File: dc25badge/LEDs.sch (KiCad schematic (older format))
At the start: 72 parts, among them U10 APA102, U11 APA102, U12 APA102, U13 APA102, U14 APA102, U15 APA102, U16 APA102, U17 APA102, U18 APA102, U19 APA102, U20 APA102, U21 APA102, U22 APA102, U23 APA102, U24 APA102, U25 APA102, U26 APA102, U27 APA102, U28 APA102, U29 APA102, U30 APA102, U31 APA102, U32 APA102, U33 APA102, U34 APA102, U35 APA102, U36 APA102, U37 APA102, U38 APA102, U39 APA102, U40 APA102, U41 APA102, U42 APA102, U43 APA102, U44 APA102, U45 APA102, U46 APA102, U47 APA102, U48 APA102, U49 APA102, U5 APA102, U50 APA102, U51 APA102, U52 APA102, U53 APA102, U54 APA102, U55 APA102, U56 APA102, U57 APA102, U58 APA102, U59 APA102, U6 APA102, U60 APA102, U61 APA102, U62 APA102, U63 APA102, U64 APA102, U7 APA102, U8 APA102, U9 APA102

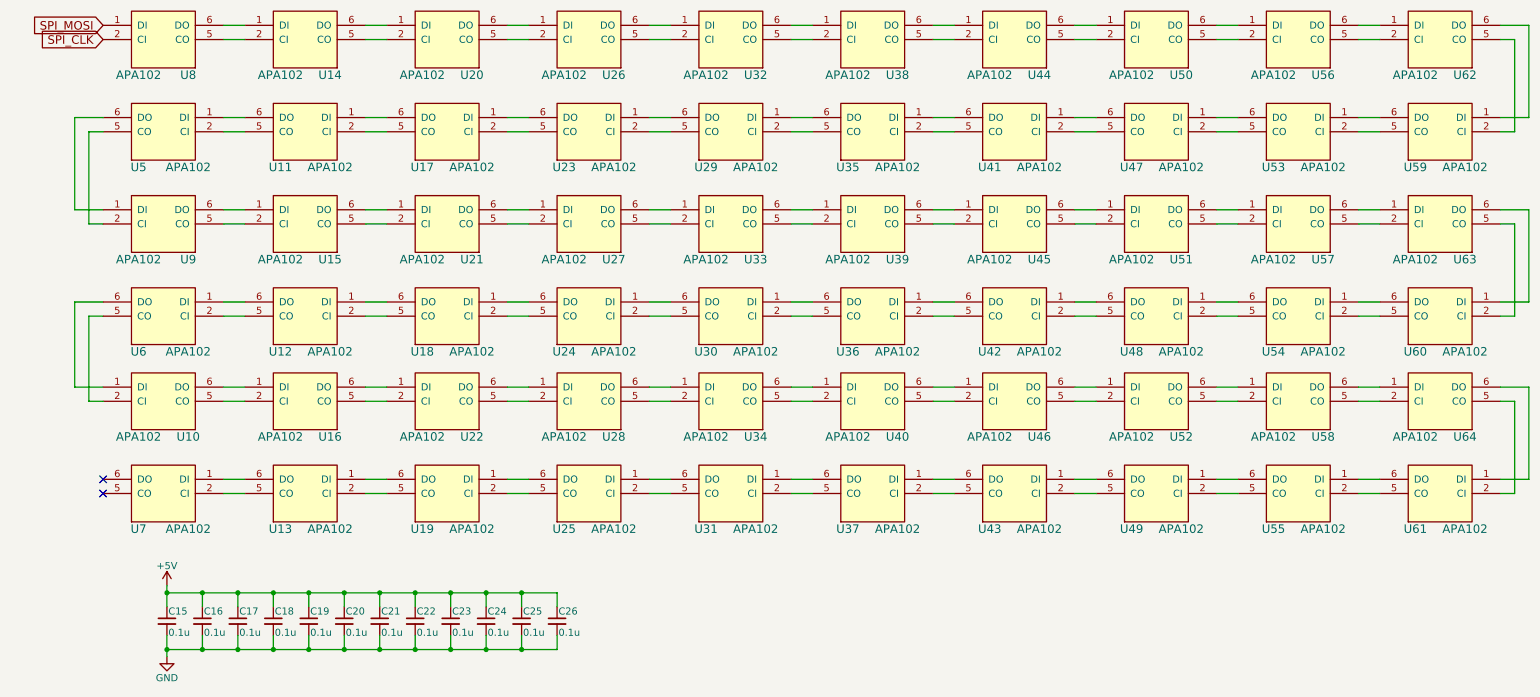
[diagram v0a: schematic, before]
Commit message: Switch to a 48-LED compact design.
Squashed commit of the following:

commit 6f3d96a4927b58100b9ba94752feefb272124e74
Author: David Tomaschik <david@systemoverlord.com>
Date:   Thu Jun 1 00:38:57 2017 -0700

    Update notes.

commit 8834e21676bcc6d408b77b676d72b46c0c38b607
Author: David Tomaschik <david@systemoverlord.com>
Date:   Thu Jun 1 00:36:52 2017 -0700

    Adjust soldermask pullback.

commit 6a323dcd490a4f291170055eb47e88aea6817de8
Author: David Tomaschik <david@systemoverlord.com>
Date:   Thu Jun 1 00:27:20 2017 -0700

    Update gerbers.

commit 7bd1ee053eeeac802e043e2ae021bc15df15862e
Author: David Tomaschik <david@systemoverlord.com>
Date:   Wed May 31 23:57:27 2017 -0700

    Silkscreen fixes.

commit dfae645180f2571b52ff98df1726defa7603401b
Author: David Tomaschik <david@systemoverlord.com>
Date:   Wed May 31 23:53:39 2017 -0700

    Remove NPTH.

commit a8849ea9e6f9fd616038fcef49a894d8de34ea94
Author: David Tomaschik <david@systemoverlord.com>
Date:   Wed May 31 23:52:01 2017 -0700

    48 LED build passes DRC.

commit 7ea769f8f5de26af904e5fc144a52ab725d91849
Author: David Tomaschik <david@systemoverlord.com>
Date:   Wed May 31 23:47:17 2017 -0700

    48 LED rebuild.

commit cfd035b7e2ebecbba1f16bb6ecda1aa97673773e
Author: David Tomaschik <david@systemoverlord.com>
Date:   Wed May 31 15:54:34 2017 -0700

    WIP

commit 41f0ca9e7d168e9e42c8a1df9409238d850c65f5
Author: David Tomaschik <david@systemoverlord.com>
Date:   Wed May 31 11:45:54 2017 -0700

    New board outline, graphics, and LED positions.

commit ffe1b2e410b22eb856250e8cd03ac130fafff124
Author: David Tomaschik <david@systemoverlord.com>
Date:   Wed May 31 09:44:54 2017 -0700

    Schematic changes for 48 LED version.
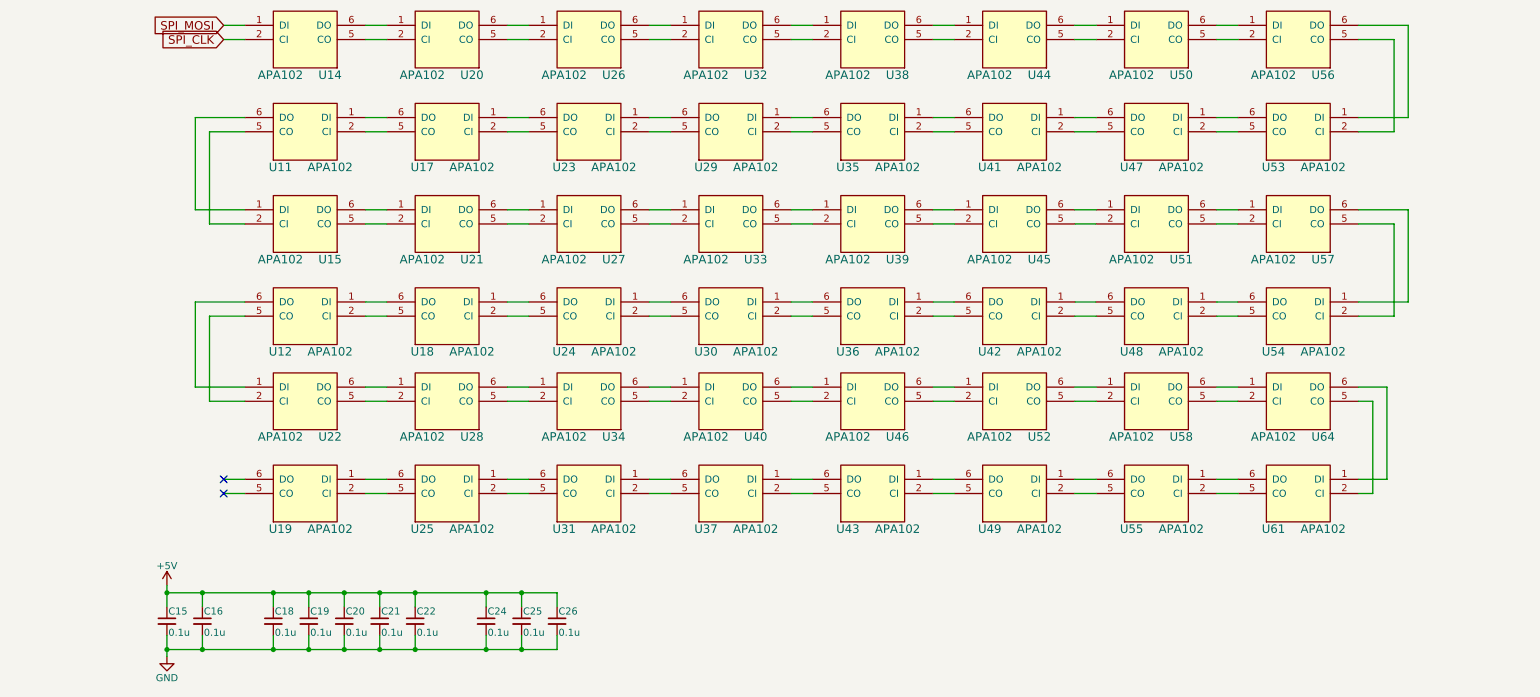
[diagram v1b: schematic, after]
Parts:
- removed C17, C23: 0.1u, Capacitors_SMD:C_0805_HandSoldering, symbol C_Small
- removed U10, U13, U16, U5, U59, U6, U60, U62, U63, U7, U8, U9: APA102, Badge_Parts:APA102, symbol APA102
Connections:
- net SPI_CLK: now also U14.2 (CI)
- net SPI_MOSI: now also U14.1 (DI)
- net at U56.5 (CO): now also U53.2 (CI)
- net at U56.6 (DO): now also U53.1 (DI)
- net at U11.5 (CO): now also U15.2 (CI)
- net at U11.6 (DO): now also U15.1 (DI)
- net at U57.5 (CO): now also U54.2 (CI)
- net at U57.6 (DO): now also U54.1 (DI)
- net at U12.5 (CO): now also U22.2 (CI)
- net at U12.6 (DO): now also U22.1 (DI)
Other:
- moved on the sheet: U19, U22, U25, U28, U31, U34, U37, U40, U43, U46, U49, U52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
